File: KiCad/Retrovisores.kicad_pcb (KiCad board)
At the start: 2 copper layers, 92 x 80 mm, 75 parts, among them J1 Conn_01x02_Pin, J10 Conn_01x07_Pin, J11 Conn_01x02_Pin, J2 DE9_Pins, J3 Conn_01x04_Pin, J4 DE9_Pins, J5 Conn_01x02_Pin, J6 Conn_01x02_Pin, J7 Conn_01x02_Pin, J8 Conn_PIC_ICSP_ICD, J9 Conn_01x04_Pin, K2 Relay_SPDT, Q14 AO3400A, Q15 AO3401A, Q16 AO3400A, Q17 AO3401A, Q18 AO3400A, Q19 AO3401A, Q20 AO3400A, Q21 AO3401A, Q22 AO3400A, Q23 AO3401A, Q24 AO3400A, Q25 AO3401A, Q27 AO3400A, SW1 SW_Push, SW2 SW_Push, SW3 SW_Push, SW4 SW_Push, SW6 SW_Nidec_CAS-120A1, U2 SN65HVD232, U4 LT1117-3.3, U5 TSR3-2450N, U7 PIC32MX250F128D-IPT, Y1 Crystal

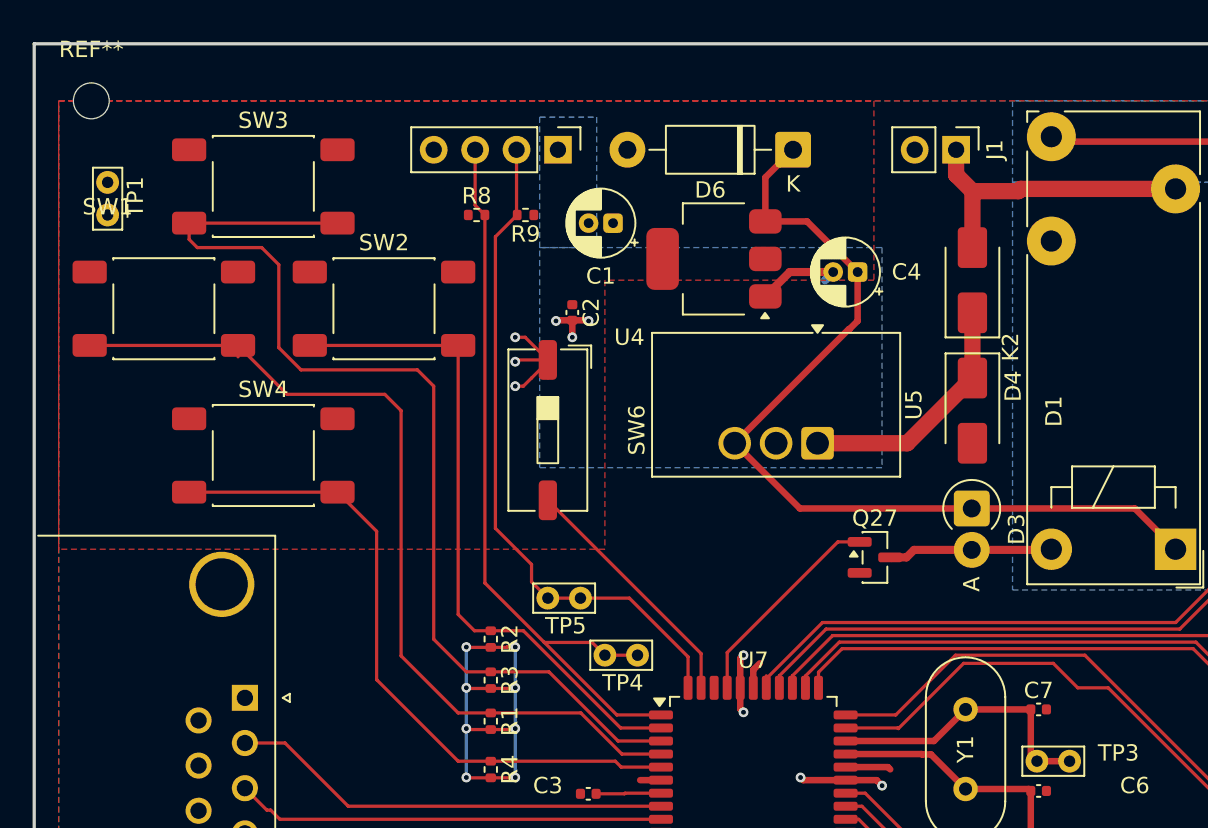
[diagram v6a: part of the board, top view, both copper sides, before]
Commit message: reorganizado el esquematico
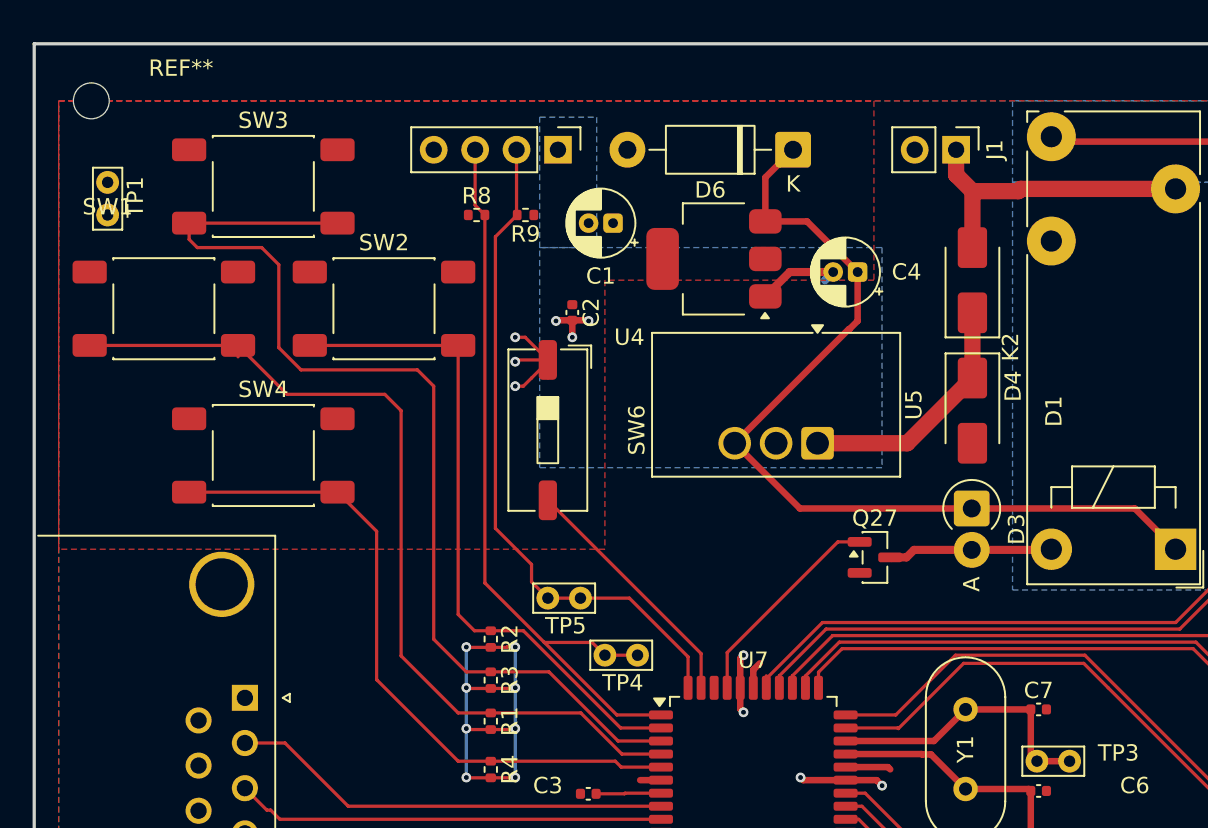
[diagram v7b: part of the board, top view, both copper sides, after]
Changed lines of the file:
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@@
 		(tags "mountinghole M2")
 		(property "Reference" "REF**"
-			(at 0 -3.15 0)
+			(at 5.5 -2 0)
 			(layer "F.SilkS")
 			(effects
@@
 	)
 	(segment
-		(start 147.5 62)
-		(end 143.5 66)
+		(start 154.868166 62)
+		(end 156.368166 63.5)
 		(width 0.2)
 		(layer "F.Cu")
@@
 	)
 	(segment
-		(start 154.5 63.5)
-		(end 156.368166 63.5)
+		(start 147.5 62)
+		(end 154.868166 62)
 		(width 0.2)
 		(layer "F.Cu")
@@
 	)
 	(segment
-		(start 143.4625 65.9625)
-		(end 140.2625 65.9625)
+		(start 143.5 66)
+		(end 147.5 62)
 		(width 0.2)
 		(layer "F.Cu")
@@
 	)
 	(segment
-		(start 167 82.5)
-		(end 177.46 82.5)
-		(width 0.2)
-		(layer "F.Cu")
-		(net 55)
-	)
-	(segment
-		(start 156.368166 63.5)
-		(end 164.434083 71.565917)
+		(start 143.4625 65.9625)
+		(end 143.5 66)
 		(width 0.2)
 		(layer "F.Cu")
@@
 	)
 	(segment
-		(start 164.434083 71.565917)
-		(end 164.434083 78.434083)
+		(start 167 82.5)
+		(end 177.46 82.5)
 		(width 0.2)
 		(layer "F.Cu")
@@
 	)
 	(segment
-		(start 154.5 63.5)
-		(end 153 62)
+		(start 156.368166 63.5)
+		(end 164.434083 71.565917)
 		(width 0.2)
 		(layer "F.Cu")
@@
 	)
 	(segment
-		(start 143.5 66)
+		(start 140.2625 65.9625)
 		(end 143.4625 65.9625)
 		(width 0.2)
@@
 	)
 	(segment
-		(start 153 62)
-		(end 147.5 62)
+		(start 164.434083 71.565917)
+		(end 164.434083 78.434083)
 		(width 0.2)
 		(layer "F.Cu")

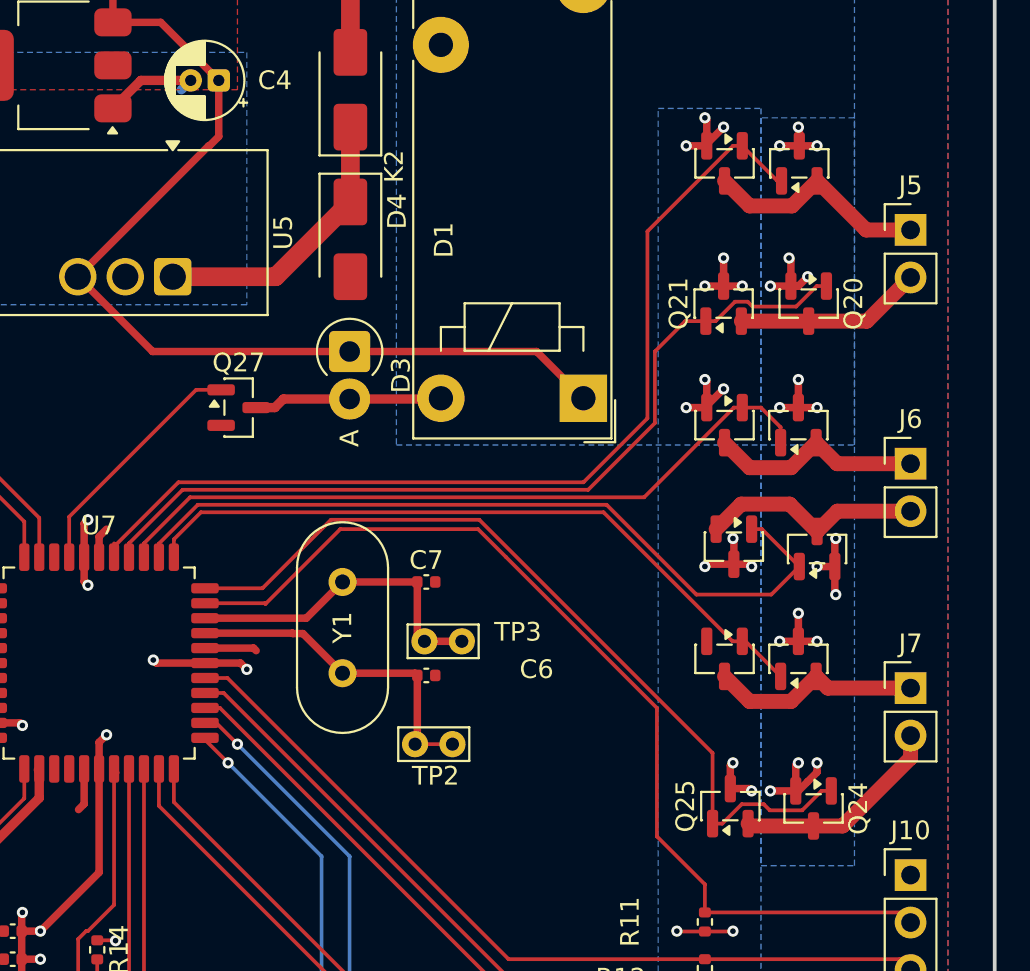
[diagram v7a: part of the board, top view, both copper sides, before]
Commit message: mosfet bien colocados
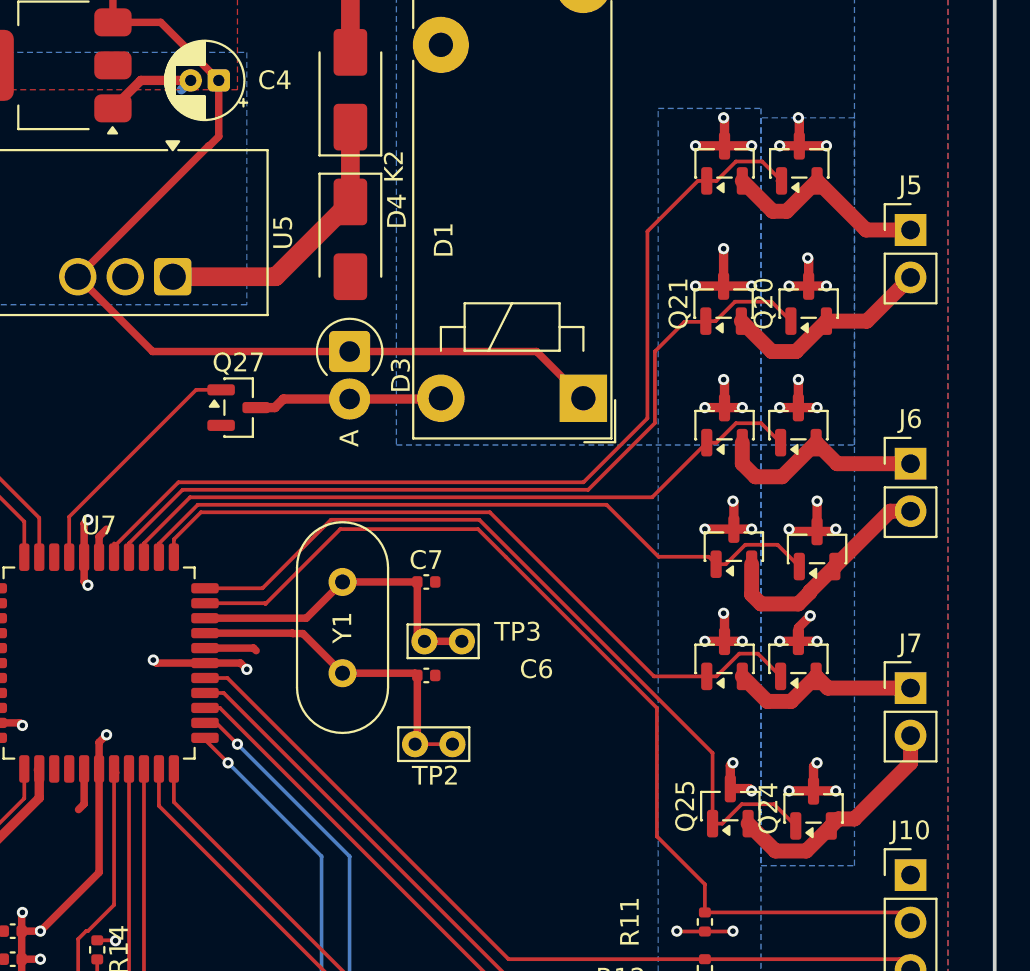
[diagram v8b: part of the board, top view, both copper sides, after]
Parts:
- turned Q15 to 90 degrees
- turned Q17 to 90 degrees
- turned Q19 to 90 degrees
- turned Q20 to 90 degrees
- turned Q23 to 90 degrees
- turned Q24 to 90 degrees
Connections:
- Q15 pad 2: GND -> Net-(J5-Pin_1)
- Q15 pad 3: Net-(J5-Pin_1) -> GND
- Q17 pad 2: GND -> Net-(J6-Pin_1)
- Q17 pad 3: Net-(J6-Pin_1) -> GND
- Q19 pad 2: GND -> Net-(J7-Pin_1)
- Q19 pad 3: Net-(J7-Pin_1) -> GND
- Q20 pad 2: VBAT -> Net-(J5-Pin_2)
- Q20 pad 3: Net-(J5-Pin_2) -> VBAT
- Q22 pad 2: VBAT -> Net-(J6-Pin_2)
- Q22 pad 3: Net-(J6-Pin_2) -> VBAT
- Q24 pad 2: VBAT -> Net-(J7-Pin_2)
- Q24 pad 3: Net-(J7-Pin_2) -> VBAT
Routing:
- net GND: track 71.4 -> 76.5 mm, vias 31 -> 34
- net SDD1: track 41.8 -> 38.1 mm
- net SDL1: track 46.2 -> 44.2 mm
- net CL: track 45.0 -> 43.0 mm
- net Net-(J5-Pin_2): track 10.0 -> 11.4 mm
- net Net-(J7-Pin_2): track 11.4 -> 12.7 mm
- net SDU1: track 39.2 -> 38.1 mm
- net OP: track 37.6 -> 38.6 mm
- net Net-(J7-Pin_1): track 11.3 -> 10.4 mm
- net Net-(J5-Pin_1): track 12.1 -> 11.4 mm
